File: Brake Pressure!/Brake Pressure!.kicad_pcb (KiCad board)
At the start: 2 copper layers, 62.4 x 54.5 mm, 17 parts, among them J1 DTF13-6P, Q1 Q_Photo_NPN_EBC, U3 MCP2515-I, U4 TJA1050DRG, X1 8MHz

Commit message: brake pressure
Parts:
- removed U3: MCP2515-I, Package_SO:SOIC-18W_7.5x11.6mm_P1.27mm
- removed U4: TJA1050DRG, Package_SO:SOIC-8_5.3x5.3mm_P1.27mm
- added REF**: Fiducial_0.75mm_Mask1.5mm, Fiducial:Fiducial_0.75mm_Mask1.5mm, F.Cu at (150.3, 109.7)
- added REF**: Fiducial_0.75mm_Mask1.5mm, Fiducial:Fiducial_0.75mm_Mask1.5mm, F.Cu at (144.8, 70.3)
- added REF**: Fiducial_0.75mm_Mask1.5mm, Fiducial:Fiducial_0.75mm_Mask1.5mm, F.Cu at (96.2, 109.7)
- added REF**: Fiducial_0.75mm_Mask1.5mm, Fiducial:Fiducial_0.75mm_Mask1.5mm, F.Cu at (102.0, 69.7)
- added U1: TJA1050DRG, Package_SO:SOIC-8_5.3x5.3mm_P1.27mm, F.Cu at (132.1, 106.0)
- added U2: MCP2515-I, Package_SO:SOIC-18W_7.5x11.6mm_P1.27mm, F.Cu at (129.2, 96.7)
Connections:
- A1 pad 5: unconnected-(A1-D2-Pad5) -> Net-(A1-D2)
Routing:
- net Net-(A1-D2): track 0.00 -> 74.5 mm
- net Net-(U3-RXCAN): track 18.2 -> 0.00 mm, vias 2 -> 0
- net Net-(U1-RXD): track 0.00 -> 18.2 mm, vias 0 -> 2
- net Net-(U3-TXCAN): track 7.29 -> 0.00 mm
- net Net-(U1-TXD): track 0.00 -> 7.29 mm

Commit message: make new connection
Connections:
- A1 pad 13: unconnected-(A1-D10-Pad13) -> CS
- A1 pad 14: unconnected-(A1-MOSI-Pad14) -> SI
- A1 pad 15: unconnected-(A1-MISO-Pad15) -> SO
- A1 pad 16: unconnected-(A1-SCK-Pad16) -> SCK

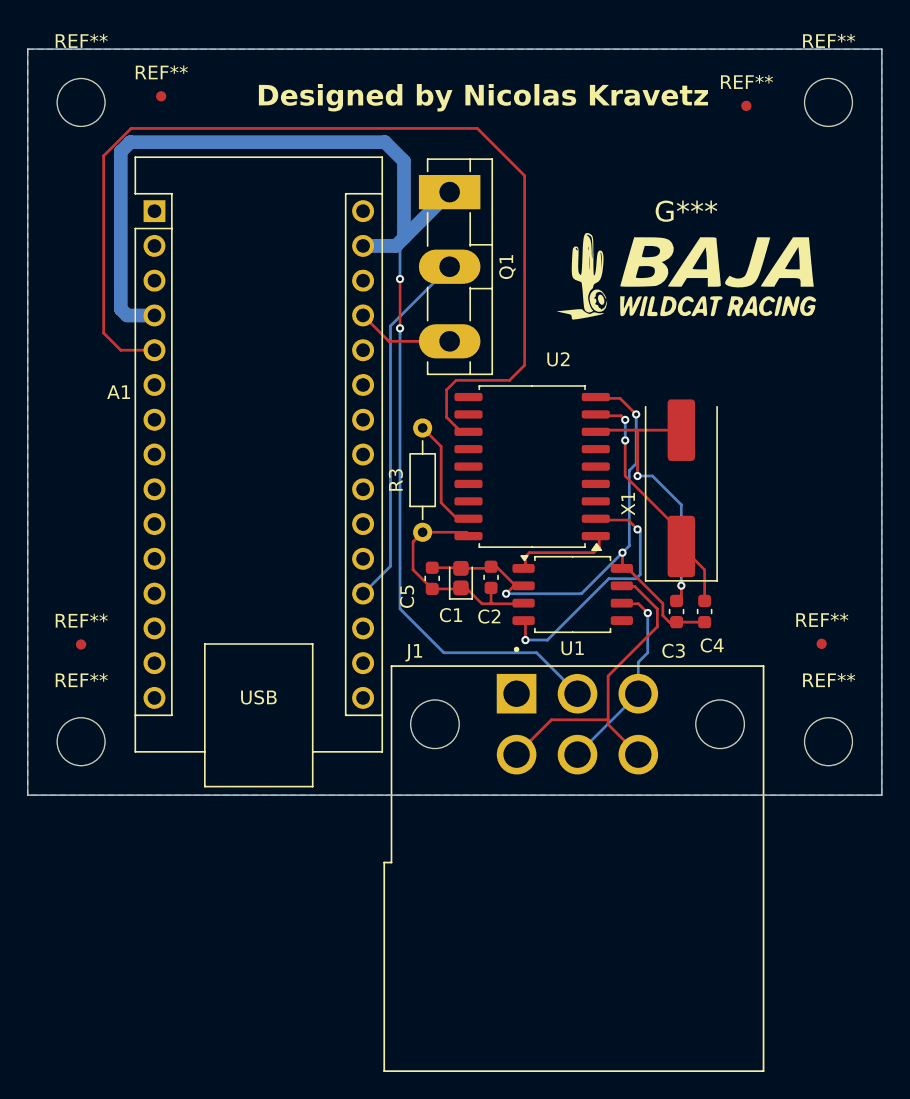
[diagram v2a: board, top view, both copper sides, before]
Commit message: brake pressure done
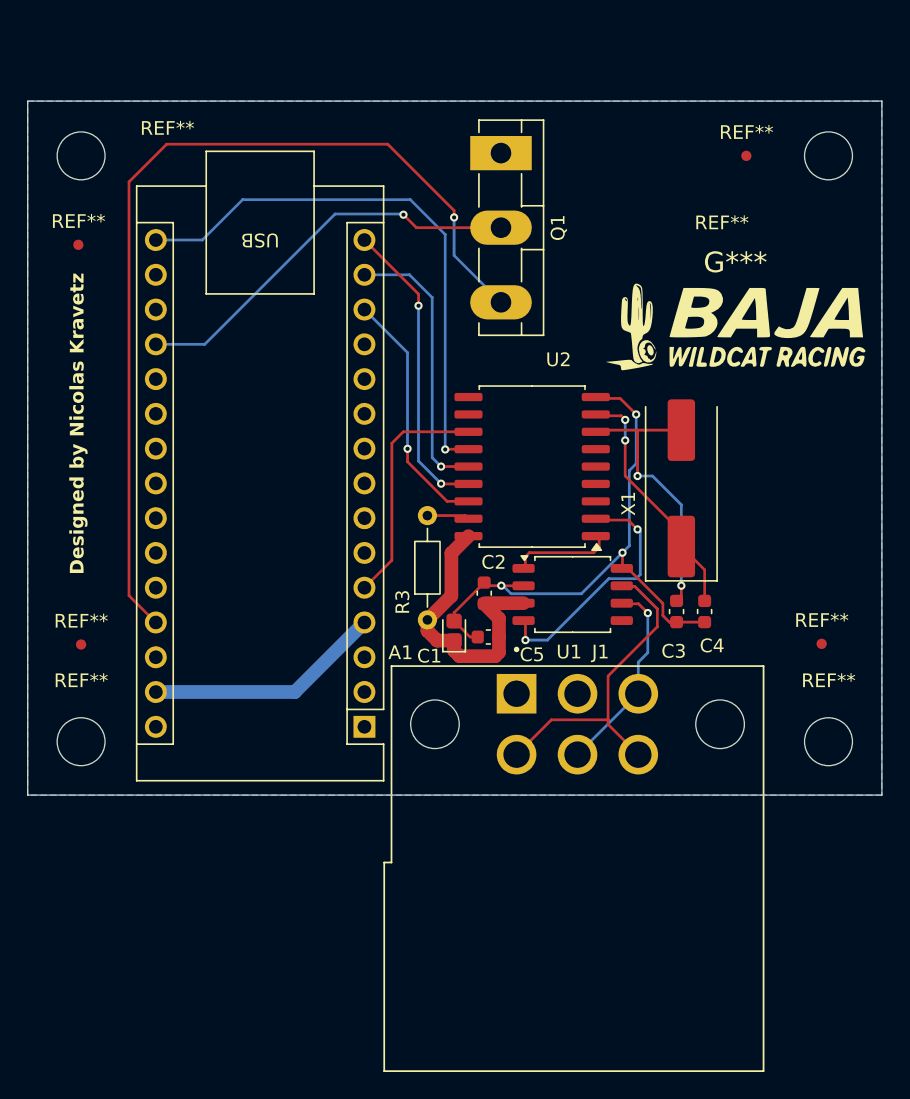
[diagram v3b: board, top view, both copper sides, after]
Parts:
- moved A1 40.7 mm to (116.9, 115.7), turned to 180 degrees
- moved REF** 12.4 mm to (96.0, 80.5)
- moved R3 6.41 mm to (121.5, 107.9)
- moved C5 5.93 mm to (126.0, 109.2), turned to 0 degrees
- moved G*** 5.16 mm to (144.0, 86.5)
- moved Q1 4.71 mm to (126.9, 73.8)
- moved REF** 3.90 mm to (150.8, 74.0)
- moved REF** 3.90 mm to (96.2, 74.0)
- moved C1 3.88 mm to (123.5, 108.7)
- moved REF** 3.65 mm to (144.8, 74.0)
- moved C2 1.26 mm to (125.7, 106.0)
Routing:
- net GND: track 91.4 -> 17.3 mm, vias 2 -> 0
- net Net-(A1-+5V): track 7.11 -> 68.0 mm, vias 0 -> 1
- net Net-(A1-D2): track 74.5 -> 17.3 mm
- net SCK: track 0.00 -> 40.8 mm, vias 0 -> 1
- net SO: track 0.00 -> 22.1 mm, vias 0 -> 2
- net SI: track 0.00 -> 20.3 mm, vias 0 -> 1
- net CS: track 0.00 -> 18.1 mm, vias 0 -> 1
- net Net-(U2-~{RESET}): track 8.80 -> 3.10 mm
- net +5V: track 17.2 -> 21.6 mm
- net Net-(A1-A0): track 26.5 -> 29.6 mm, vias 0 -> 1
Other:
- board size 62.4 x 54.5 mm -> 62.4 x 50.7 mm
